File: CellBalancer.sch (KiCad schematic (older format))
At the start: 14 parts, among them IC2 MAX923, Q2 IRF7455PBF

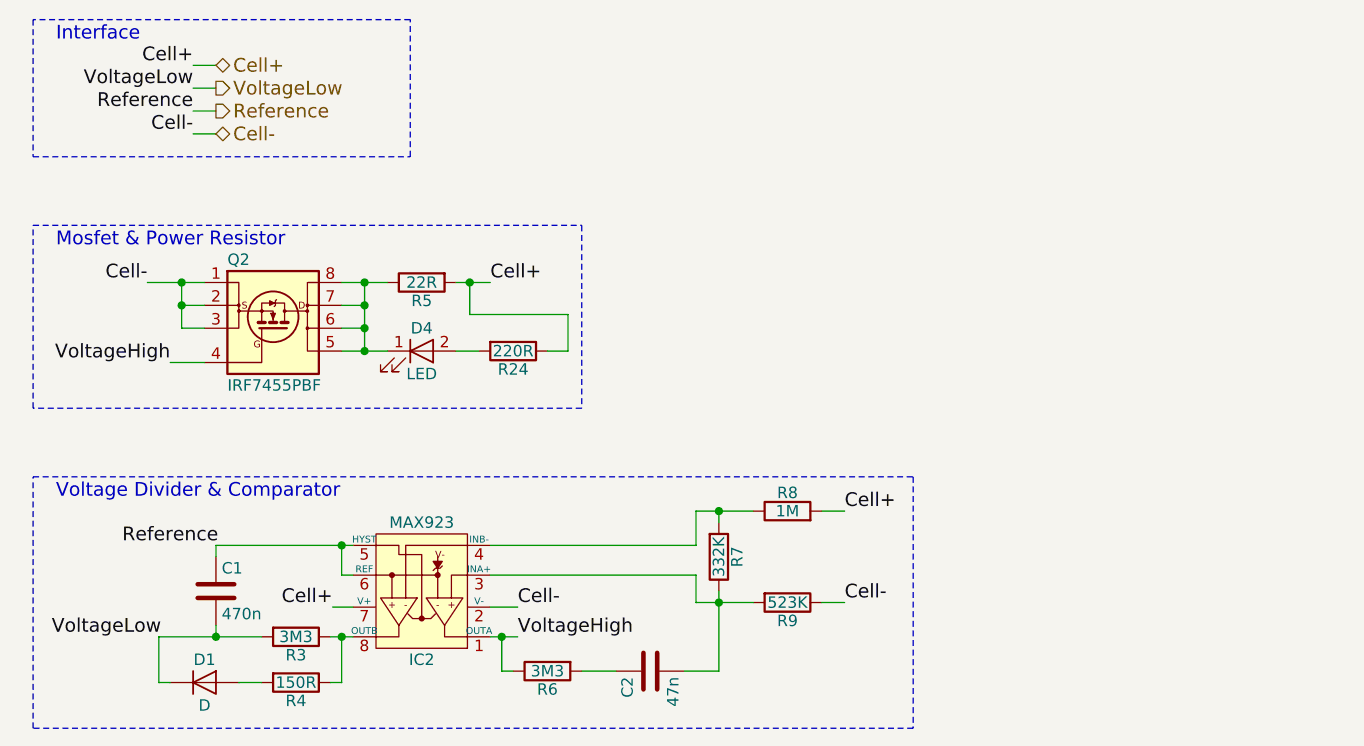
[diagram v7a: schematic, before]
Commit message: updated pull ups on quad comparator to 1M, update center divider resistor to 340K to be closer to 4.2V charge cutoff
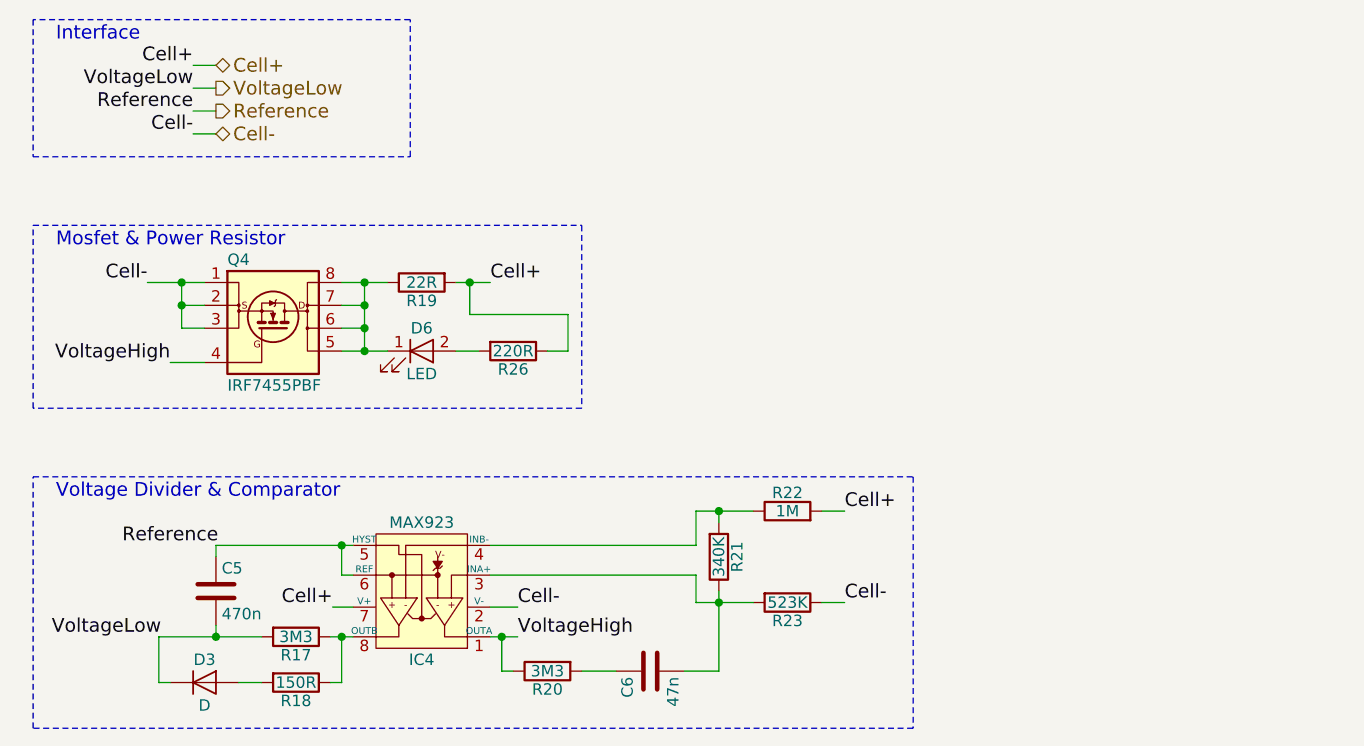
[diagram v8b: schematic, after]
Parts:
- R7: value 332K -> 340K
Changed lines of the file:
@@
 AR Path="/58CDE720/58CDB997" Ref="Q3"  Part="1"
 AR Path="/58CDEEA6/58CDB997" Ref="Q4"  Part="1"
-F 0 "Q2" H 1950 2450 50  0000 L CNN
+F 0 "Q4" H 1950 2450 50  0000 L CNN
 F 1 "IRF7455PBF" H 1950 1900 50  0000 L CNN
 F 2 "Housings_SOIC:SOIC-8_3.9x4.9mm_Pitch1.27mm" H 2160 1740 50  0001 C CIN
@@
 AR Path="/58CDE720/58CDB9A6" Ref="R12"  Part="1"
 AR Path="/58CDEEA6/58CDB9A6" Ref="R19"  Part="1"
-F 0 "R5" V 2880 1950 50  0000 C CNN
+F 0 "R19" V 2880 1950 50  0000 C CNN
 F 1 "22R" V 2800 1950 50  0000 C CNN
 F 2 "balancer:R_0612" V 2730 1950 50  0001 C CNN
@@
 AR Path="/58CDE720/58CD80F2" Ref="R15"  Part="1"
 AR Path="/58CDEEA6/58CD80F2" Ref="R22"  Part="1"
-F 0 "R8" V 4480 2950 50  0000 C CNN
+F 0 "R22" V 4480 2950 50  0000 C CNN
 F 1 "1M" V 4400 2950 50  0000 C CNN
 F 2 "Resistors_SMD:R_0805" V 4330 2950 50  0001 C CNN
@@
 AR Path="/58CDE720/58CD8143" Ref="R14"  Part="1"
 AR Path="/58CDEEA6/58CD8143" Ref="R21"  Part="1"
-F 0 "R7" V 4180 3150 50  0000 C CNN
-F 1 "332K" V 4100 3150 50  0000 C CNN
+F 0 "R21" V 4180 3150 50  0000 C CNN
+F 1 "340K" V 4100 3150 50  0000 C CNN
 F 2 "Resistors_SMD:R_0805" V 4030 3150 50  0001 C CNN
 F 3 "" H 4100 3150 50  0001 C CNN
@@
 AR Path="/58CDE720/58CD819C" Ref="R16"  Part="1"
 AR Path="/58CDEEA6/58CD819C" Ref="R23"  Part="1"
-F 0 "R9" V 4480 3350 50  0000 C CNN
+F 0 "R23" V 4480 3350 50  0000 C CNN
 F 1 "523K" V 4400 3350 50  0000 C CNN
 F 2 "Resistors_SMD:R_0805" V 4330 3350 50  0001 C CNN
@@
 AR Path="/58CDE720/58CD8827" Ref="IC3"  Part="1"
 AR Path="/58CDEEA6/58CD8827" Ref="IC4"  Part="1"
-F 0 "IC2" H 2800 3600 50  0000 C CNN
+F 0 "IC4" H 2800 3600 50  0000 C CNN
 F 1 "MAX923" H 2800 3000 50  0000 C CNN
 F 2 "Housings_SOIC:SOIC-8_3.9x4.9mm_Pitch1.27mm" H 2810 2830 60  0001 C CIN
@@
 AR Path="/58CDE720/58CDBF0F" Ref="R13"  Part="1"
 AR Path="/58CDEEA6/58CDBF0F" Ref="R20"  Part="1"
-F 0 "R6" V 3430 3650 50  0000 C CNN
+F 0 "R20" V 3430 3650 50  0000 C CNN
 F 1 "3M3" V 3350 3650 50  0000 C CNN
 F 2 "Resistors_SMD:R_0805" V 3280 3650 50  0001 C CNN
@@
 AR Path="/58CDE720/58CDBF54" Ref="C4"  Part="1"
 AR Path="/58CDEEA6/58CDBF54" Ref="C6"  Part="1"
-F 0 "C2" H 3825 3750 50  0000 L CNN
+F 0 "C6" H 3825 3750 50  0000 L CNN
 F 1 "47n" H 3825 3550 50  0000 L CNN
 F 2 "Capacitors_SMD:C_0805" H 3838 3500 50  0001 C CNN
@@
 AR Path="/58CDE720/58CDD170" Ref="R10"  Part="1"
 AR Path="/58CDEEA6/58CDD170" Ref="R17"  Part="1"
-F 0 "R3" V 2330 3500 50  0000 C CNN
+F 0 "R17" V 2330 3500 50  0000 C CNN
 F 1 "3M3" V 2250 3500 50  0000 C CNN
 F 2 "Resistors_SMD:R_0805" V 2180 3500 50  0001 C CNN
@@
 AR Path="/58CDE720/58CDD1EC" Ref="R11"  Part="1"
 AR Path="/58CDEEA6/58CDD1EC" Ref="R18"  Part="1"
-F 0 "R4" V 2330 3700 50  0000 C CNN
+F 0 "R18" V 2330 3700 50  0000 C CNN
 F 1 "150R" V 2250 3700 50  0000 C CNN
 F 2 "Resistors_SMD:R_0805" V 2180 3700 50  0001 C CNN
@@
 AR Path="/58CDE720/58CDD221" Ref="D2"  Part="1"
 AR Path="/58CDEEA6/58CDD221" Ref="D3"  Part="1"
-F 0 "D1" H 1850 3800 50  0000 C CNN
+F 0 "D3" H 1850 3800 50  0000 C CNN
 F 1 "D" H 1850 3600 50  0000 C CNN
 F 2 "balancer:D_0805" H 1850 3700 50  0001 C CNN
@@
 AR Path="/58CDE720/58CDD43A" Ref="C3"  Part="1"
 AR Path="/58CDEEA6/58CDD43A" Ref="C5"  Part="1"
-F 0 "C1" H 1925 3400 50  0000 L CNN
+F 0 "C5" H 1925 3400 50  0000 L CNN
 F 1 "470n" H 1925 3200 50  0000 L CNN
 F 2 "Capacitors_SMD:C_0805" H 1938 3150 50  0001 C CNN
@@
 AR Path="/58CDE720/58CFD09E" Ref="R25"  Part="1"
 AR Path="/58CDEEA6/58CFD09E" Ref="R26"  Part="1"
-F 0 "R24" V 3280 2250 50  0000 C CNN
+F 0 "R26" V 3280 2250 50  0000 C CNN
 F 1 "220R" V 3200 2250 50  0000 C CNN
 F 2 "Resistors_SMD:R_0805" V 3130 2250 50  0001 C CNN
@@
 AR Path="/58CDE720/58CFD291" Ref="D5"  Part="1"
 AR Path="/58CDEEA6/58CFD291" Ref="D6"  Part="1"
-F 0 "D4" H 2800 2350 50  0000 C CNN
+F 0 "D6" H 2800 2350 50  0000 C CNN
 F 1 "LED" H 2800 2150 50  0000 C CNN
 F 2 "LEDs:LED_0805" H 2800 2250 50  0001 C CNN
